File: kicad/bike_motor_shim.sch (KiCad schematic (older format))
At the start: 12 parts, among them J1 Conn_01x06_Male, J2 Conn_01x06_Male, K1 MSxx-1Axx-75, U1 ATtiny45-20SU, U2 MCP1700-5002E_SOT23, Y1 Crystal_Small

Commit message: Fixed relay footprint
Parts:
- K1: footprint Relay_THT:Relay_SPST_StandexMeder_MS_Form1AB -> Relay_THT:Relay_SPST_StandexMeder_SIL_Form1A
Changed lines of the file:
@@
 EESchema Schematic File Version 4
+LIBS:bike_motor_shim-cache
 EELAYER 26 0
 EELAYER END
@@
 F 0 "K1" H 6080 3946 50  0000 L CNN
 F 1 "MSxx-1Axx-75" H 6080 3855 50  0000 L CNN
-F 2 "Relay_THT:Relay_SPST_StandexMeder_MS_Form1AB" H 6100 3850 50  0001 L CNN
+F 2 "Relay_THT:Relay_SPST_StandexMeder_SIL_Form1A" H 6100 3850 50  0001 L CNN
 F 3 "https://standexelectronics.com/de/produkte/ms-reed-relais/" H 5750 3900 50  0001 C CNN
 	1    5750 3900

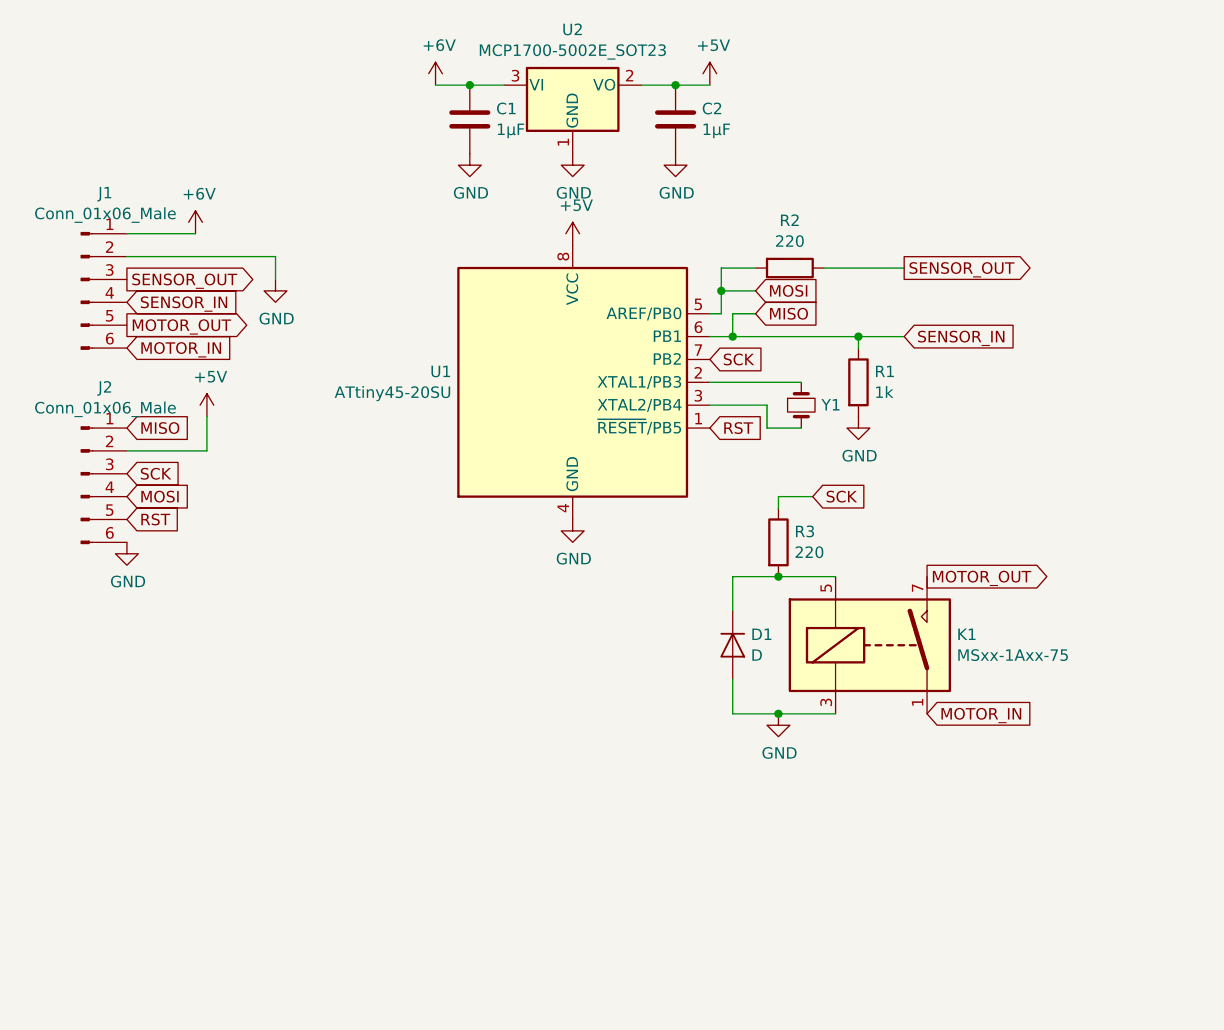
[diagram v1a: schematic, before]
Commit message: Adding bypass relay and LEDs.
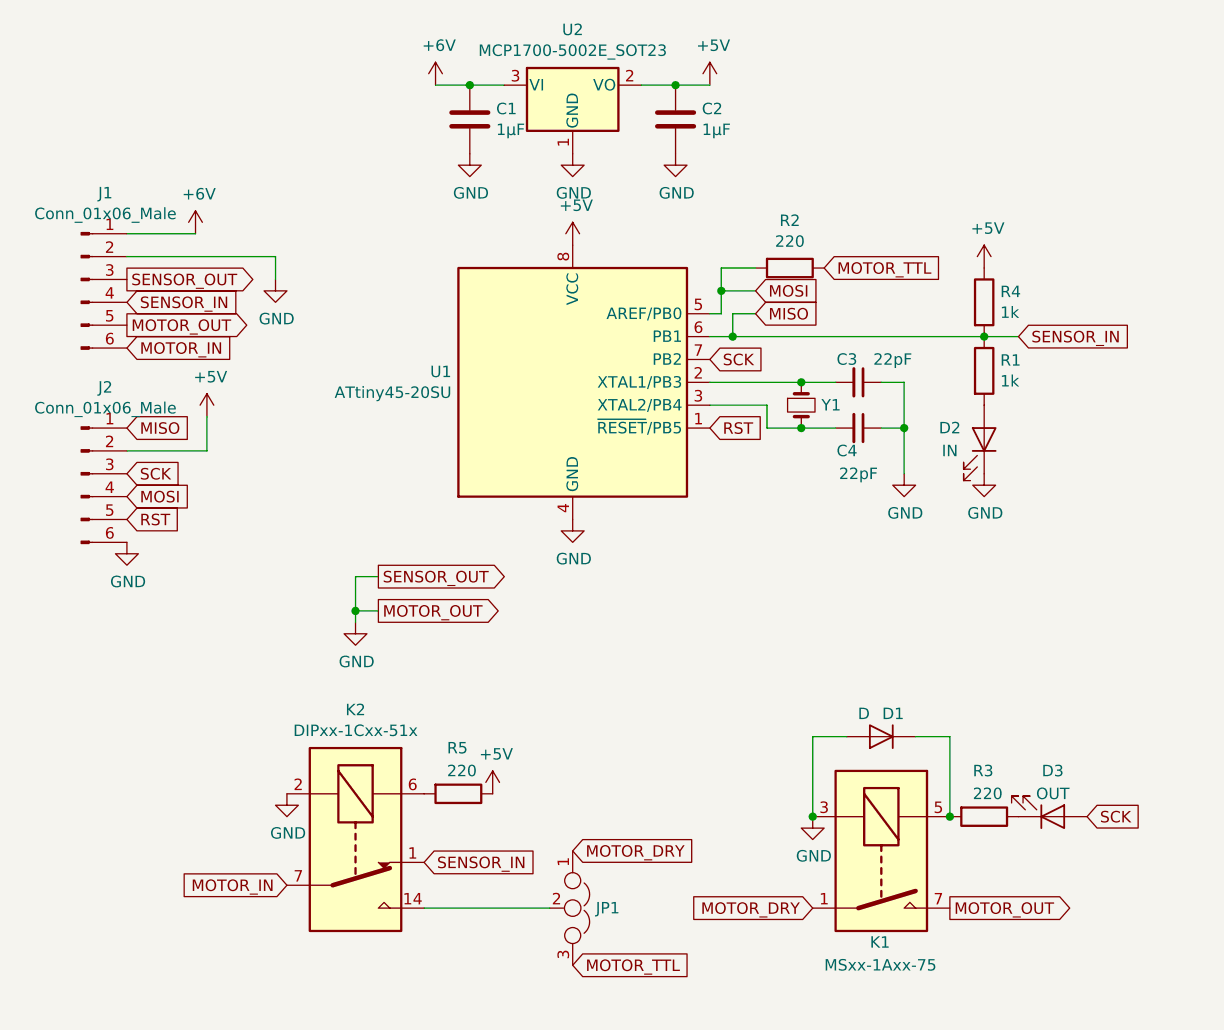
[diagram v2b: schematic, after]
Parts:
- added C3, C4: 22pF, Capacitor_SMD:C_0805_2012Metric_Pad1.15x1.40mm_HandSolder, symbol Device:C_Small
- added D2: IN, LED_SMD:LED_0805_2012Metric_Pad1.15x1.40mm_HandSolder, symbol Device:LED
- added D3: OUT, LED_SMD:LED_0805_2012Metric_Pad1.15x1.40mm_HandSolder, symbol Device:LED
- added JP1: Jumper_NC_Dual, Connector_PinHeader_2.54mm:PinHeader_1x03_P2.54mm_Vertical, symbol Device:Jumper_NC_Dual
- added K2: DIPxx-1Cxx-51x, trr-relay:TRR-RELAY-SMDIP-14_W7.62mm, symbol Relay:DIPxx-1Cxx-51x
- added R4: 1k, Resistor_SMD:R_0805_2012Metric_Pad1.15x1.40mm_HandSolder, symbol Device:R
- added R5: 220, Resistor_SMD:R_0805_2012Metric_Pad1.15x1.40mm_HandSolder, symbol Device:R
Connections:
- net MOTOR_OUT is gone; now on net GND: J1.5 (Pin_5), K1.7
- net +5V: now also R4.1, R5.1
- net GND: now also J1.3 (Pin_3), C3.1, C4.1, D2.1 (K), K2.2; no longer R1.2
- net MISO: now also K2.1, R4.2
- net MOTOR_IN: now also K2.7, K2.8; no longer K1.1
- net SCK: now also D3.2 (A); no longer R3.1
- net at U1.2 (XTAL1/PB3), Y1.1: now also C3.2
- net at U1.3 (XTAL2/PB4), Y1.2: now also C4.2
- net SENSOR_OUT renamed MOTOR_TTL
- net MOTOR_TTL: now also JP1.3; no longer J1.3 (Pin_3)
- new net: D2.2 (A), R1.2
- new net: D3.1 (K), R3.1
- new net: JP1.2, K2.14
- new net: K2.6, R5.2
- new net MOTOR_DRY: JP1.1, K1.1
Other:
- moved on the sheet: D1, K1, R1, R3

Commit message: Board and sketch improvements.
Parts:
- removed K2: DIPxx-1Cxx-51x, trr-relay:TRR-RELAY-SMDIP-14_W7.62mm, symbol Relay:DIPxx-1Cxx-51x
- removed R5: 220, Resistor_SMD:R_0805_2012Metric_Pad1.15x1.40mm_HandSolder, symbol Device:R
- added K2: G6K-2, Relay_SMD:Relay_DPDT_Omron_G6K-2F-Y, symbol relay_omron_g6k-2:G6K-2
- added Q1: S8050, Package_TO_SOT_SMD:SOT-23, symbol Transistor_BJT:BC817
- D1: footprint Diode_SMD:D_SMA_Handsoldering -> Diode_SMD:D_SMA
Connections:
- net +5V: now also D1.1 (K), K1.5, K2.1
- net GND: now also K1.1, K2.8, Q1.2 (E); no longer D1.2 (A), K1.3, K1.7
- net MISO: now also K2.5; no longer J1.4 (Pin_4)
- net MOTOR_DRY: now also K1.7; no longer K1.1
- net MOTOR_IN: now also K2.3, K2.7
- net at R3.1: now also Q1.1 (B); no longer D3.1 (K)
- net at JP1.2: now also K2.4
- new net: D1.2 (A), K1.3, Q1.3 (C)
- new net: D3.1 (K), R3.2
- new net SENSOR_IN: J1.4 (Pin_4), K2.2, K2.6
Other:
- moved on the sheet: D1, D3, JP1, K1, R3
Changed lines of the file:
@@
 L Device:D D1
 U 1 1 5CFFD5FF
-P 5750 4300
-F 0 "D1" H 5650 4200 50  0000 L CNN
-F 1 "D" H 5800 4200 50  0000 L CNN
-F 2 "Diode_SMD:D_SMA_Handsoldering" H 5750 4300 50  0001 C CNN
-F 3 "~" H 5750 4300 50  0001 C CNN
-	1    5750 4300
-	-1   0    0    1
+P 5750 4500
+F 0 "D1" H 5650 4400 50  0000 L CNN
+F 1 "D" H 5800 4400 50  0000 L CNN
+F 2 "Diode_SMD:D_SMA" H 5750 4500 50  0001 C CNN
+F 3 "~" H 5750 4500 50  0001 C CNN
+	1    5750 4500
+	0    1    1    0
 $EndComp
 $Comp
@@
 L Device:R R3
 U 1 1 5CFFDB4E
-P 6200 4650
-F 0 "R3" V 6000 4600 50  0000 L CNN
-F 1 "220" V 6100 4600 50  0000 L CNN
-F 2 "Resistor_SMD:R_0805_2012Metric_Pad1.15x1.40mm_HandSolder" V 6130 4650 50  0001 C CNN
-F 3 "~" H 6200 4650 50  0001 C CNN
-	1    6200 4650
+P 5650 5000
+F 0 "R3" V 5450 4950 50  0000 L CNN
+F 1 "220" V 5550 4950 50  0000 L CNN
+F 2 "Resistor_SMD:R_0805_2012Metric_Pad1.15x1.40mm_HandSolder" V 5580 5000 50  0001 C CNN
+F 3 "~" H 5650 5000 50  0001 C CNN
+	1    5650 5000
 	0    1    1    0
 $EndComp
@@
 L Relay:MSxx-1Axx-75 K1
 U 1 1 5CFFE000
-P 5750 4850
-F 0 "K1" V 6100 4800 50  0000 L CNN
-F 1 "MSxx-1Axx-75" V 6200 4600 50  0000 L CNN
-F 2 "Relay_THT:Relay_SPST_StandexMeder_SIL_Form1A" H 6100 4800 50  0001 L CNN
-F 3 "https://standexelectronics.com/de/produkte/ms-reed-relais/" H 5750 4850 50  0001 C CNN
-	1    5750 4850
-	0    1    1    0
+P 6300 4500
+F 0 "K1" V 6650 4450 50  0000 L CNN
+F 1 "MSxx-1Axx-75" V 6750 4250 50  0000 L CNN
+F 2 "Relay_THT:Relay_SPST_StandexMeder_SIL_Form1A" H 6650 4450 50  0001 L CNN
+F 3 "https://standexelectronics.com/de/produkte/ms-reed-relais/" H 6300 4500 50  0001 C CNN
+	1    6300 4500
+	1    0    0    -1
 $EndComp
 $Comp
@@
 L power:GND #PWR0108
 U 1 1 5CFFE5F9
-P 5450 4650
-F 0 "#PWR0108" H 5450 4400 50  0001 C CNN
-F 1 "GND" H 5455 4477 50  0000 C CNN
-F 2 "" H 5450 4650 50  0001 C CNN
-F 3 "" H 5450 4650 50  0001 C CNN
-	1    5450 4650
+P 6500 4800
+F 0 "#PWR0108" H 6500 4550 50  0001 C CNN
+F 1 "GND" H 6505 4627 50  0000 C CNN
+F 2 "" H 6500 4800 50  0001 C CNN
+F 3 "" H 6500 4800 50  0001 C CNN
+	1    6500 4800
 	1    0    0    -1
 $EndComp
@@
 	1    0    0    -1
 $EndComp
-Text GLabel 6050 5050 2    50   Output ~ 0
-MOTOR_OUT
-Text GLabel 2450 2500 2    50   Output ~ 0
-MOTOR_OUT
 $Comp
 L power:GND #PWR0114
 U 1 1 5D00050E
-P 3100 2300
-F 0 "#PWR0114" H 3100 2050 50  0001 C CNN
-F 1 "GND" H 3105 2127 50  0000 C CNN
-F 2 "" H 3100 2300 50  0001 C CNN
-F 3 "" H 3100 2300 50  0001 C CNN
-	1    3100 2300
-	1    0    0    -1
-$EndComp
-Text GLabel 2450 2300 2    50   Output ~ 0
-SENSOR_OUT
+P 3100 2700
+F 0 "#PWR0114" H 3100 2450 50  0001 C CNN
+F 1 "GND" H 3105 2527 50  0000 C CNN
+F 2 "" H 3100 2700 50  0001 C CNN
+F 3 "" H 3100 2700 50  0001 C CNN
+	1    3100 2700
+	1    0    0    -1
+$EndComp
 Text GLabel 2450 2400 2    50   Input ~ 0
 SENSOR_IN
 Wire Wire Line
 	2450 2100 2750 2100
-Text GLabel 6650 4650 2    50   Input ~ 0
-SCK
-Text GLabel 6350 2550 2    50   Input ~ 0
-SENSOR_IN
 Wire Wire Line
 	5000 2550 5100 2550
@@
 	2450 2200 3100 2200
 Wire Wire Line
-	3100 2200 3100 2300
-Wire Wire Line
 	5000 2450 5050 2450
 Wire Wire Line
@@
 	5050 2250 5050 2350
 Connection ~ 5050 2350
-Text GLabel 3550 3750 2    50   Output ~ 0
-MOTOR_OUT
-$Comp
-L power:GND #PWR0113
-U 1 1 5D1F994C
-P 3450 3800
-F 0 "#PWR0113" H 3450 3550 50  0001 C CNN
-F 1 "GND" H 3455 3627 50  0000 C CNN
-F 2 "" H 3450 3800 50  0001 C CNN
-F 3 "" H 3450 3800 50  0001 C CNN
-	1    3450 3800
-	1    0    0    -1
-$EndComp
-Wire Wire Line
-	3450 3750 3550 3750
-Text GLabel 3550 3600 2    50   Output ~ 0
-SENSOR_OUT
-Wire Wire Line
-	3550 3600 3450 3600
-Wire Wire Line
-	3450 3600 3450 3750
-Connection ~ 3450 3750
-Wire Wire Line
-	3450 3750 3450 3800
-$Comp
-L Relay:DIPxx-1Cxx-51x K2
-U 1 1 5D1FA5BE
-P 3450 4750
-F 0 "K2" V 2883 4750 50  0000 C CNN
-F 1 "DIPxx-1Cxx-51x" V 2974 4750 50  0000 C CNN
-F 2 "trr-relay:TRR-RELAY-SMDIP-14_W7.62mm" H 3900 4700 50  0001 L CNN
-F 3 "https://standexelectronics.com/wp-content/uploads/datasheet_reed_relay_DIP.pdf" H 3450 4750 50  0001 C CNN
-	1    3450 4750
-	0    1    1    0
-$EndComp
-Text GLabel 3750 4850 2    50   Input ~ 0
-SENSOR_IN
-Text GLabel 3150 4950 0    50   Input ~ 0
-MOTOR_IN
-$Comp
-L Device:R R5
-U 1 1 5D1FAE17
-P 3900 4550
-F 0 "R5" V 3700 4500 50  0000 L CNN
-F 1 "220" V 3800 4500 50  0000 L CNN
-F 2 "Resistor_SMD:R_0805_2012Metric_Pad1.15x1.40mm_HandSolder" V 3830 4550 50  0001 C CNN
-F 3 "~" H 3900 4550 50  0001 C CNN
-	1    3900 4550
-	0    1    1    0
-$EndComp
-$Comp
-L power:GND #PWR0115
-U 1 1 5D1FB4BA
-P 3150 4550
-F 0 "#PWR0115" H 3150 4300 50  0001 C CNN
-F 1 "GND" H 3155 4377 50  0000 C CNN
-F 2 "" H 3150 4550 50  0001 C CNN
-F 3 "" H 3150 4550 50  0001 C CNN
-	1    3150 4550
-	1    0    0    -1
-$EndComp
-$Comp
-L power:+5V #PWR0116
-U 1 1 5D1FB4E1
-P 4050 4550
-F 0 "#PWR0116" H 4050 4400 50  0001 C CNN
-F 1 "+5V" H 4065 4723 50  0000 C CNN
-F 2 "" H 4050 4550 50  0001 C CNN
-F 3 "" H 4050 4550 50  0001 C CNN
-	1    4050 4550
-	1    0    0    -1
-$EndComp
 $Comp
 L Device:LED D3
 U 1 1 5D1FCA35
-P 6500 4650
-F 0 "D3" H 6500 4450 50  0000 C CNN
-F 1 "OUT" H 6500 4550 50  0000 C CNN
-F 2 "LED_SMD:LED_0805_2012Metric_Pad1.15x1.40mm_HandSolder" H 6500 4650 50  0001 C CNN
-F 3 "~" H 6500 4650 50  0001 C CNN
-	1    6500 4650
-	1    0    0    1
-$EndComp
-Wire Wire Line
-	5600 4300 5450 4300
-Wire Wire Line
-	5450 4300 5450 4650
-Connection ~ 5450 4650
-Wire Wire Line
-	5900 4300 6050 4300
-Wire Wire Line
-	6050 4300 6050 4650
-Connection ~ 6050 4650
+P 5350 5000
+F 0 "D3" H 5350 4800 50  0000 C CNN
+F 1 "OUT" H 5350 4900 50  0000 C CNN
+F 2 "LED_SMD:LED_0805_2012Metric_Pad1.15x1.40mm_HandSolder" H 5350 5000 50  0001 C CNN
+F 3 "~" H 5350 5000 50  0001 C CNN
+	1    5350 5000
+	-1   0    0    -1
+$EndComp
 $Comp
 L Device:LED D2
@@
 	1    0    0    -1
 $EndComp
-Wire Wire Line
-	6350 2550 6200 2550
 Connection ~ 5100 2550
 Connection ~ 6200 2550
@@
 Text GLabel 5500 2250 2    50   Input ~ 0
 MOTOR_TTL
-Text GLabel 5450 5050 0    50   Input ~ 0
+Text GLabel 6550 4100 2    50   Input ~ 0
 MOTOR_DRY
 Wire Wire Line
@@
 L Device:Jumper_NC_Dual JP1
 U 1 1 5D20A5FA
-P 4400 5050
-F 0 "JP1" V 4400 5151 50  0000 L CNN
-F 1 "Jumper_NC_Dual" V 4445 5151 50  0001 L CNN
-F 2 "Connector_PinHeader_2.54mm:PinHeader_1x03_P2.54mm_Vertical" H 4400 5050 50  0001 C CNN
-F 3 "~" H 4400 5050 50  0001 C CNN
-	1    4400 5050
-	0    1    1    0
-$EndComp
-Text GLabel 4400 4800 2    50   Input ~ 0
+P 4400 5000
+F 0 "JP1" V 4400 5101 50  0000 L CNN
+F 1 "Jumper_NC_Dual" V 4445 5101 50  0001 L CNN
+F 2 "Connector_PinHeader_2.54mm:PinHeader_1x03_P2.54mm_Vertical" H 4400 5000 50  0001 C CNN
+F 3 "~" H 4400 5000 50  0001 C CNN
+	1    4400 5000
+	0    1    1    0
+$EndComp
+Text GLabel 4400 4750 2    50   Input ~ 0
 MOTOR_DRY
-Text GLabel 4400 5300 2    50   Input ~ 0
+Text GLabel 4400 5250 2    50   Input ~ 0
 MOTOR_TTL
-Wire Wire Line
-	3750 5050 4300 5050
+$Comp
+L relay_omron_g6k-2:G6K-2 K2
+U 1 1 5D3F7A92
+P 3500 4900
+F 0 "K2" V 2733 4900 50  0000 C CNN
+F 1 "G6K-2" V 2824 4900 50  0000 C CNN
+F 2 "Relay_SMD:Relay_DPDT_Omron_G6K-2F-Y" H 4150 4850 50  0001 L CNN
+F 3 "http://omronfs.omron.com/en_US/ecb/products/pdf/en-g6k.pdf" H 3300 4900 50  0001 C CNN
+	1    3500 4900
+	0    1    1    0
+$EndComp
+Text GLabel 3200 4900 0    50   Input ~ 0
+MOTOR_IN
+Text GLabel 3800 4800 2    50   Input ~ 0
+SENSOR_IN
+Text GLabel 3200 5300 0    50   Input ~ 0
+SENSOR_IN
+Text GLabel 3800 5400 2    50   Input ~ 0
+MISO
+Text GLabel 3800 5200 2    50   Input ~ 0
+MOTOR_IN
+$Comp
+L power:GND #PWR0113
+U 1 1 5D3F7DCA
+P 3200 4500
+F 0 "#PWR0113" H 3200 4250 50  0001 C CNN
+F 1 "GND" H 3205 4327 50  0000 C CNN
+F 2 "" H 3200 4500 50  0001 C CNN
+F 3 "" H 3200 4500 50  0001 C CNN
+	1    3200 4500
+	1    0    0    -1
+$EndComp
+$Comp
+L power:+5V #PWR0115
+U 1 1 5D3F7E4A
+P 3800 4500
+F 0 "#PWR0115" H 3800 4350 50  0001 C CNN
+F 1 "+5V" H 3815 4673 50  0000 C CNN
+F 2 "" H 3800 4500 50  0001 C CNN
+F 3 "" H 3800 4500 50  0001 C CNN
+	1    3800 4500
+	1    0    0    -1
+$EndComp
+Wire Wire Line
+	3800 5000 4300 5000
+$Comp
+L Transistor_BJT:BC817 Q1
+U 1 1 5D3F9D7A
+P 6000 5000
+F 0 "Q1" H 6191 5046 50  0000 L CNN
+F 1 "S8050" H 6191 4955 50  0000 L CNN
+F 2 "Package_TO_SOT_SMD:SOT-23" H 6200 4925 50  0001 L CIN
+F 3 "http://www.unisonic.com.tw/datasheet/S8050.pdf" H 6000 5000 50  0001 L CNN
+	1    6000 5000
+	1    0    0    -1
+$EndComp
+$Comp
+L power:+5V #PWR0116
+U 1 1 5D3F9DE7
+P 6100 4200
+F 0 "#PWR0116" H 6100 4050 50  0001 C CNN
+F 1 "+5V" H 6115 4373 50  0000 C CNN
+F 2 "" H 6100 4200 50  0001 C CNN
+F 3 "" H 6100 4200 50  0001 C CNN
+	1    6100 4200
+	1    0    0    -1
+$EndComp
+Text GLabel 5200 5000 0    50   Input ~ 0
+SCK
+$Comp
+L power:GND #PWR0119
+U 1 1 5D3FB8A4
+P 6100 5200
+F 0 "#PWR0119" H 6100 4950 50  0001 C CNN
+F 1 "GND" H 6105 5027 50  0000 C CNN
+F 2 "" H 6100 5200 50  0001 C CNN
+F 3 "" H 6100 5200 50  0001 C CNN
+	1    6100 5200
+	1    0    0    -1
+$EndComp
+Wire Wire Line
+	5750 4350 5750 4200
+Wire Wire Line
+	5750 4200 6100 4200
+Wire Wire Line
+	5750 4650 5750 4800
+Wire Wire Line
+	5750 4800 6100 4800
+Wire Wire Line
+	6500 4200 6500 4100
+Wire Wire Line
+	6500 4100 6550 4100
+Wire Wire Line
+	2450 2300 3100 2300
+Wire Wire Line
+	3100 2200 3100 2300
+Connection ~ 3100 2300
+Wire Wire Line
+	3100 2300 3100 2500
+Wire Wire Line
+	2450 2500 3100 2500
+Connection ~ 3100 2500
+Wire Wire Line
+	3100 2500 3100 2700
+Connection ~ 6100 4800
+Connection ~ 6100 4200
 $EndSCHEMATC
